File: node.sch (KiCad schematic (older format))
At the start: 27 parts, among them SW1 Reset, U1 NCP703, U2 LD39130S, U3 LPS25HB, U4 Si7006-A20, U5 ESP-12E, U6 ISL29035

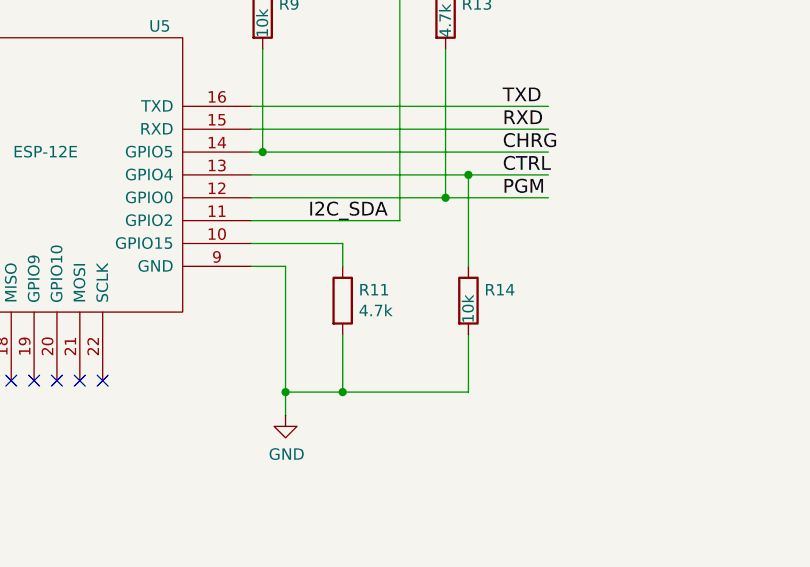
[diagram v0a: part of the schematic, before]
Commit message: Remove extra resistor on CTRL
On branch master
modified:   TLPHnodeV2.net
modified:   node.sch
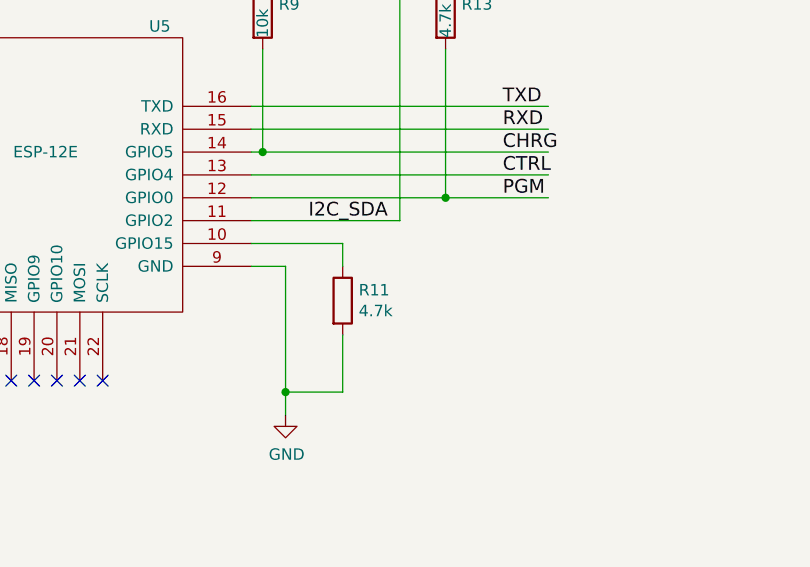
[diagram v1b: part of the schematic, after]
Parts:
- removed R14: 10k, Resistors_SMD:R_0603, symbol R
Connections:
- wire segments 104 -> 102
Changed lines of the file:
@@
-$EndComp
-$Comp
-L R R14
-U 1 1 583BD5E7
-P 8150 5150
-F 0 "R14" H 8220 5196 50  0000 L CNN
-F 1 "10k" V 8150 5050 50  0000 L CNN
-F 2 "Resistors_SMD:R_0603" V 8080 5150 50  0001 C CNN
-F 3 "" H 8150 5150 50  0000 C CNN
-	1    8150 5150
-	1    0    0    -1
 $EndComp
 $Comp
@@
 Wire Wire Line
 	7600 5300 7600 5550
-Wire Wire Line
-	7350 5550 8150 5550
 Connection ~ 7350 5550
 Wire Wire Line
@@
 Connection ~ 7250 4500
 Wire Wire Line
-	8150 5550 8150 5300
-Connection ~ 7600 5550
-Wire Wire Line
-	8150 5000 8150 4600
-Connection ~ 8150 4600
-Wire Wire Line
 	1400 3350 2400 3350
 Wire Wire Line
 	4200 6600 4200 6650
 Connection ~ 4200 6600
+Wire Wire Line
+	7600 5550 7350 5550
 $EndSCHEMATC

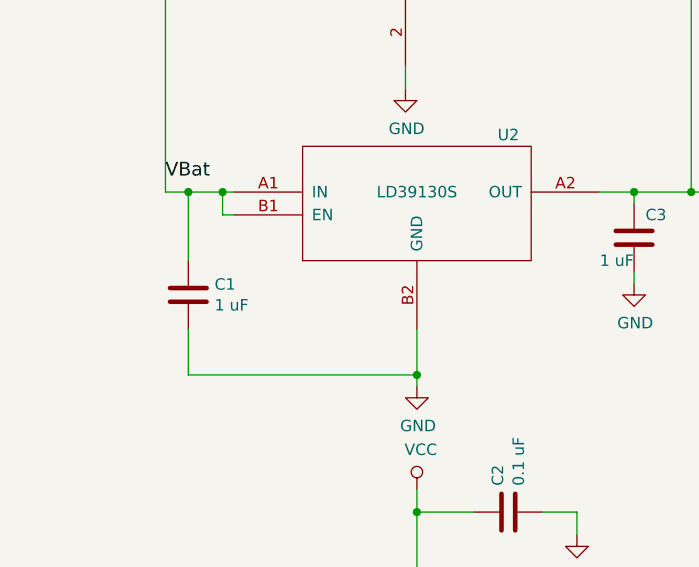
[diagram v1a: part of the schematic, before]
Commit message: Remove C1
    - C8 should be adequate for both the regulators (U1, U2) and the
      charger (U7)
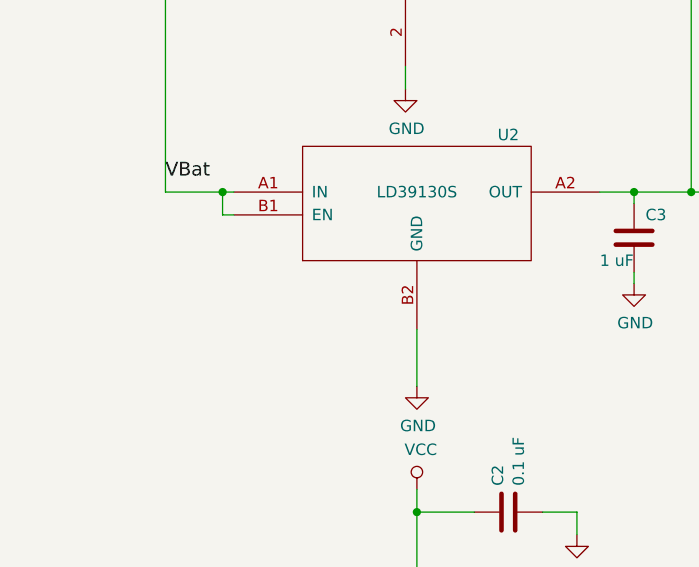
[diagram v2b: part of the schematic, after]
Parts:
- removed C1: 1 uF, Capacitors_SMD:C_0603, symbol C
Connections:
- wire segments 102 -> 99
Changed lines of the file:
@@
-$EndComp
-$Comp
-L C C1
-U 1 1 583BE628
-P 1400 3000
-F 0 "C1" H 1515 3046 50  0000 L CNN
-F 1 "1 uF" H 1515 2955 50  0000 L CNN
-F 2 "Capacitors_SMD:C_0603" H 1438 2850 50  0001 C CNN
-F 3 "" H 1400 3000 50  0000 C CNN
-	1    1400 3000
-	1    0    0    -1
 $EndComp
 $Comp
@@
 	3350 2950 3350 2900
 Wire Wire Line
-	1400 2550 1400 2850
-Connection ~ 1400 2550
-Wire Wire Line
-	1400 3150 1400 3350
-Wire Wire Line
 	1600 2650 1550 2650
 Wire Wire Line
@@
 Wire Wire Line
 	2400 3150 2400 3400
-Connection ~ 2400 3350
 Wire Wire Line
 	1550 1400 1300 1400
@@
 Connection ~ 7250 4500
 Wire Wire Line
-	1400 3350 2400 3350
-Wire Wire Line
 	4200 6600 4200 6650

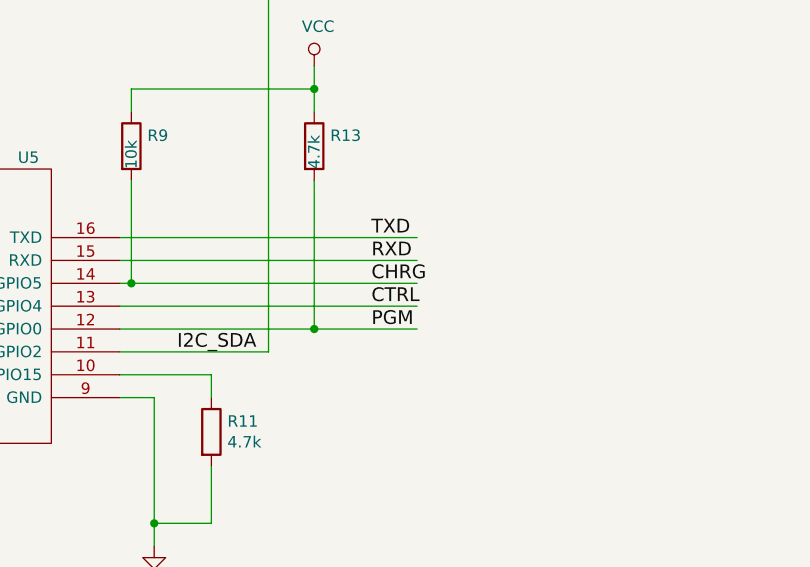
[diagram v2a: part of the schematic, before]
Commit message: Swap ESP-8266 signals for charger control
    - Swap CHRG and CTRL to make layout cleaner

On branch master
modified:   TLPHnodeV2.kicad_pcb
modified:   TLPHnodeV2.net
modified:   node.sch
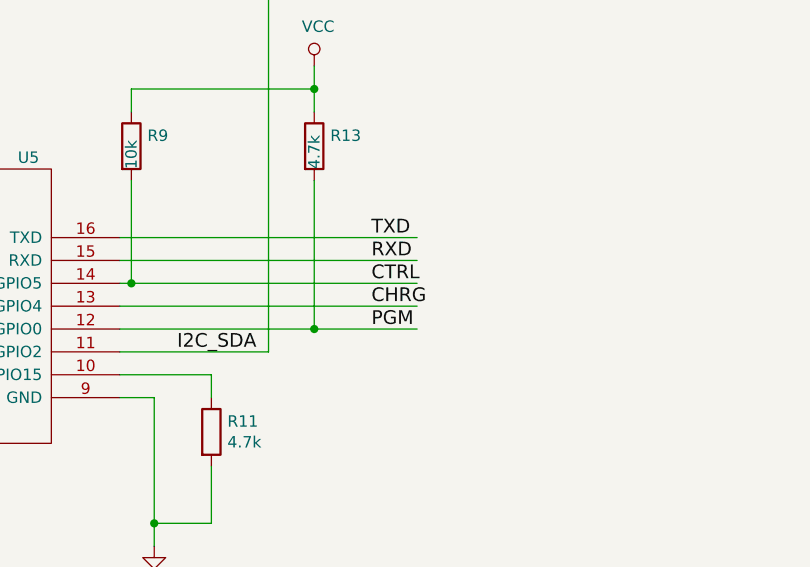
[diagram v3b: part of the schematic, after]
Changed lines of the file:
@@
 Text Label 3600 6500 0    60   ~ 0
 CHRG
-Text Label 8300 4500 0    60   ~ 0
-CHRG
-Text Label 8300 4600 0    60   ~ 0
-CTRL
 Text HLabel 3550 6100 0    60   Input ~ 0
 TXD
@@
 Wire Wire Line
 	7600 5550 7350 5550
+Text Label 8300 4500 0    60   ~ 0
+CTRL
+Text Label 8300 4600 0    60   ~ 0
+CHRG
 $EndSCHEMATC
